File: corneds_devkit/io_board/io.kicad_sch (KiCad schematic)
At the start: 0 parts

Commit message: added switch footprint, io sch, and keypad IC footprint. Need to find new LEDs and make joystick footprint
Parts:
- added J1: Conn_02x10_Counter_Clockwise, Connector_PinHeader_1.27mm:PinHeader_2x10_P1.27mm_Horizontal, symbol Connector_Generic:Conn_02x10_Counter_Clockwise
- added J2, J3: Conn_01x03_Pin, Connector_PinHeader_1.27mm:PinHeader_1x03_P1.27mm_Vertical, symbol Connector:Conn_01x03_Pin
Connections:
- new net GNDL: J1.10 (Pin_10)
- new net GNDR: J1.11 (Pin_11)
- new net SCLL: J1.6 (Pin_6)
- new net SCLR: J1.15 (Pin_15)
- new net SDAL: J1.5 (Pin_5)
- new net SDAR: J1.16 (Pin_16)
- new net VDD_3V3L: J1.2 (Pin_2), J2.1 (Pin_1)
- new net VDD_3V3R: J1.19 (Pin_19), J3.3 (Pin_3)
- new net VDD_5VL: J1.1 (Pin_1), J2.3 (Pin_3)
- new net VDD_5VR: J1.20 (Pin_20), J3.1 (Pin_1)
- new net VJOYL: J2.2 (Pin_2)
- new net VJOYR: J3.2 (Pin_2)
- new net left_led_di: J1.3 (Pin_3)
- new net mouse_x: J1.13 (Pin_13)
- new net mouse_y: J1.14 (Pin_14)
- new net nINTL: J1.4 (Pin_4)
- new net nINTR: J1.17 (Pin_17)
- new net nRESET: J1.9 (Pin_9)
- new net right_led_di: J1.18 (Pin_18)
- new net scroll_x: J1.8 (Pin_8)
- new net scroll_y: J1.7 (Pin_7)

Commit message: io sch done. Need to route
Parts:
- added J4: nOEL_en, Connector_PinHeader_1.00mm:PinHeader_1x02_P1.00mm_Vertical, symbol Connector:Conn_01x02_Pin
- added J5: nOER_en, Connector_PinHeader_1.00mm:PinHeader_1x02_P1.00mm_Vertical, symbol Connector:Conn_01x02_Pin
- added R10, R4, R6, R8: 20k, Resistor_SMD:R_0402_1005Metric, symbol Device:R
- added R3, R5, R7, R9: 10k, Resistor_SMD:R_0402_1005Metric, symbol Device:R
- added U5, U6: TXB0102DCU, Package_SO:VSSOP-8_2.4x2.1mm_P0.5mm, symbol Logic_LevelTranslator:TXB0102DCU
- J2: value Conn_01x03_Pin -> JOYL_VSEL
- J3: value Conn_01x03_Pin -> JOYR_VSEL
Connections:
- net GNDL: now also J4.2 (Pin_2), R4.2, R6.2, U5.2 (GND)
- net GNDR: now also J5.1 (Pin_1), R10.2, R8.2, U6.2 (GND)
- net VDD_3V3L: now also U5.3 (VCCA)
- net VDD_3V3R: now also U6.3 (VCCA)
- net VDD_5VL: now also U5.7 (VCCB)
- net VDD_5VR: now also U6.7 (VCCB)
- net left_led_di: now also U5.8 (B1); no longer J1.3 (Pin_3)
- net mouse_x: now also R9.1; no longer J1.13 (Pin_13)
- net mouse_y: now also R7.1; no longer J1.14 (Pin_14)
- net right_led_di: now also U6.8 (B1); no longer J1.18 (Pin_18)
- net scroll_x: now also R5.1; no longer J1.8 (Pin_8)
- net scroll_y: now also R3.1; no longer J1.7 (Pin_7)
- new net: J1.8 (Pin_8), R3.2, R4.1
- new net: J1.3 (Pin_3), U5.5 (A1)
- new net: J4.1 (Pin_1), U5.6 (OE)
- new net: J1.7 (Pin_7), R5.2, R6.1
- new net: J1.13 (Pin_13), R10.1, R9.2
- new net: J1.14 (Pin_14), R7.2, R8.1
- new net: J1.18 (Pin_18), U6.5 (A1)
- new net: J5.2 (Pin_2), U6.6 (OE)
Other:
- moved on the sheet: J1, J2, J3

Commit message: finished routing power board and started on control board schematic but realized I need seperate reset lines
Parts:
- J1: footprint Connector_PinHeader_1.27mm:PinHeader_2x10_P1.27mm_Horizontal -> Connector_PinHeader_1.27mm:PinHeader_2x10_P1.27mm_Vertical
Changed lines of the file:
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@@
 			)
 		)
-		(property "Footprint" "Connector_PinHeader_1.27mm:PinHeader_2x10_P1.27mm_Horizontal"
+		(property "Footprint" "Connector_PinHeader_1.27mm:PinHeader_2x10_P1.27mm_Vertical"
 			(at 157.48 63.5 0)
 			(effects

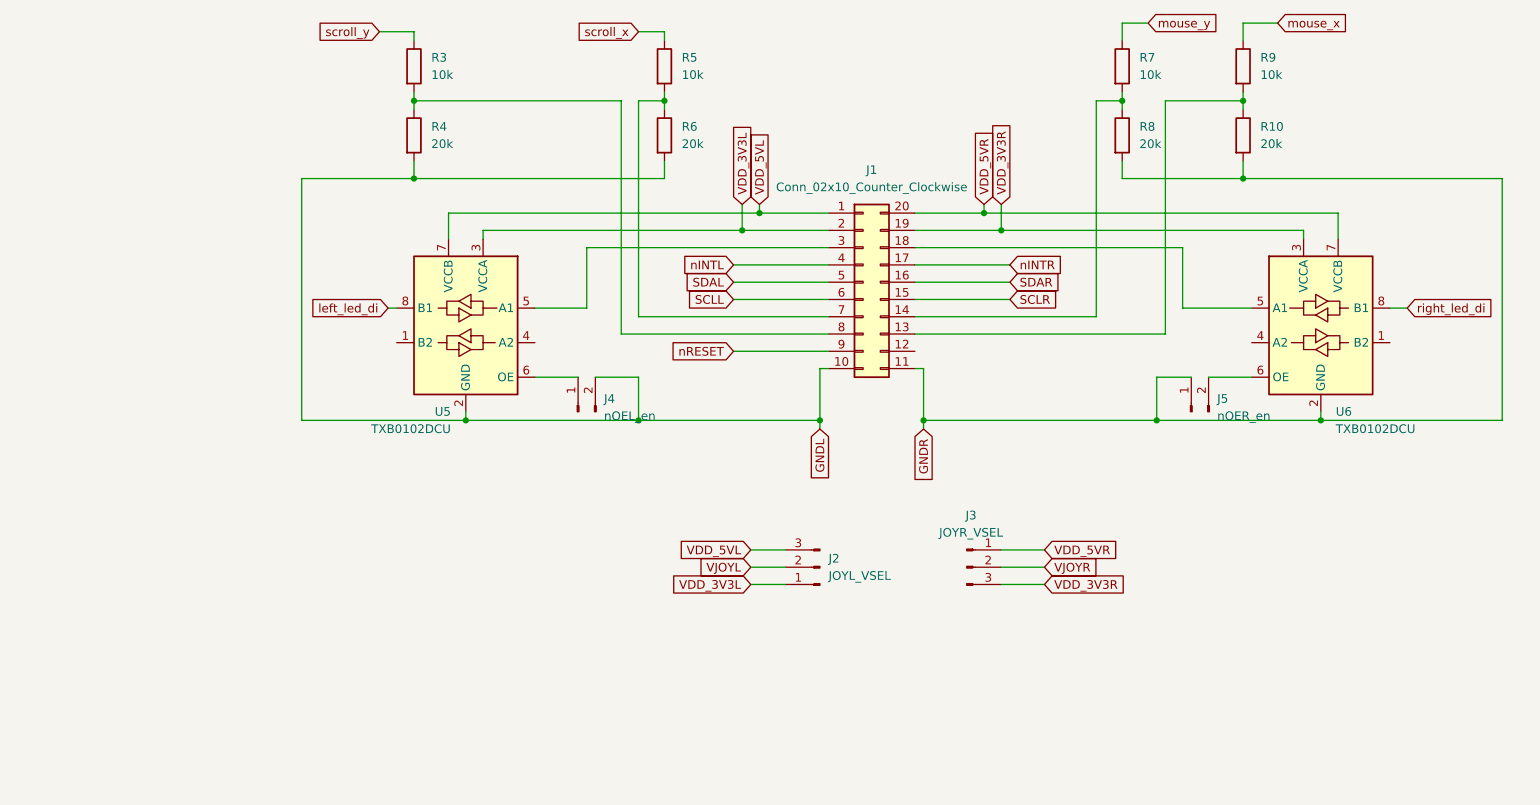
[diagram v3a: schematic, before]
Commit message: ordered devkit rev A
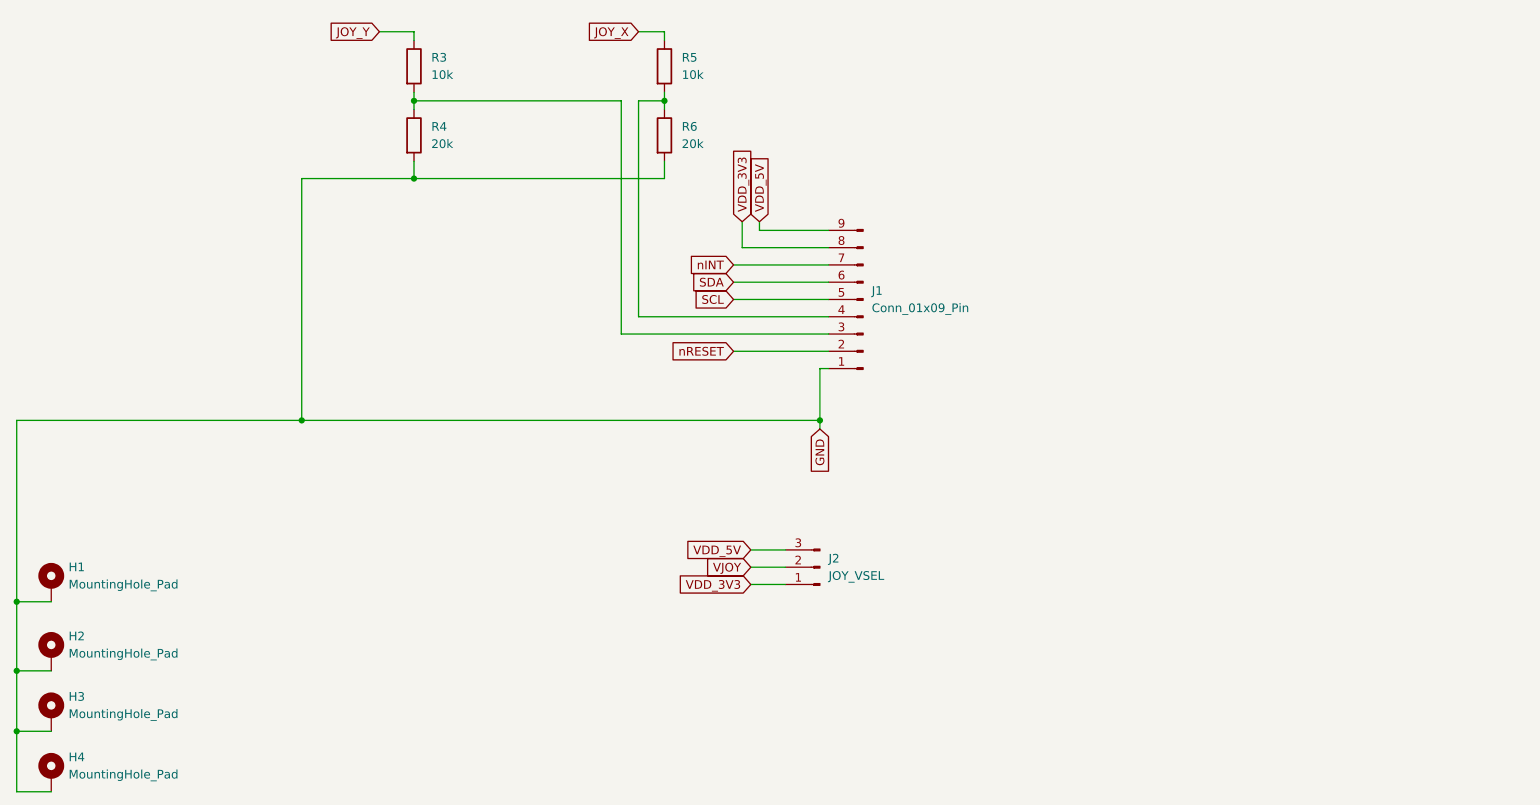
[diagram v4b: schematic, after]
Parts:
- removed J1: Conn_02x10_Counter_Clockwise, Connector_PinHeader_1.27mm:PinHeader_2x10_P1.27mm_Vertical, symbol Connector_Generic:Conn_02x10_Counter_Clockwise
- removed J3: JOYR_VSEL, Connector_PinHeader_1.27mm:PinHeader_1x03_P1.27mm_Vertical, symbol Connector:Conn_01x03_Pin
- removed J4: nOEL_en, Connector_PinHeader_1.00mm:PinHeader_1x02_P1.00mm_Vertical, symbol Connector:Conn_01x02_Pin
- removed J5: nOER_en, Connector_PinHeader_1.00mm:PinHeader_1x02_P1.00mm_Vertical, symbol Connector:Conn_01x02_Pin
- removed R10, R8: 20k, Resistor_SMD:R_0402_1005Metric, symbol Device:R
- removed R7, R9: 10k, Resistor_SMD:R_0402_1005Metric, symbol Device:R
- removed U5, U6: TXB0102DCU, Package_SO:VSSOP-8_2.4x2.1mm_P0.5mm, symbol Logic_LevelTranslator:TXB0102DCU
- added H1, H2, H3, H4: MountingHole_Pad, MountingHole:MountingHole_3.2mm_M3_Pad_Via, symbol Mechanical:MountingHole_Pad
- added J1: Conn_01x09_Pin, Connector_PinHeader_1.27mm:PinHeader_1x09_P1.27mm_Vertical, symbol Connector:Conn_01x09_Pin
- J2: value JOYL_VSEL -> JOY_VSEL
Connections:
- net nRESET: now also J1.2 (Pin_2)
- net at R3.2, R4.1: now also J1.3 (Pin_3)
- net at R5.2, R6.1: now also J1.4 (Pin_4)
- net GNDL renamed GND
- net GND: now also H1.1, H2.1, H3.1, H4.1, J1.1 (Pin_1)
- net VDD_3V3L renamed VDD_3V3
- net VDD_3V3: now also J1.8 (Pin_8)
- net VDD_5VL renamed VDD_5V
- net VDD_5V: now also J1.9 (Pin_9)
- net VJOYL renamed VJOY
- net scroll_x renamed JOY_X
- net scroll_y renamed JOY_Y
- new net SCL: J1.5 (Pin_5)
- new net SDA: J1.6 (Pin_6)
- new net nINT: J1.7 (Pin_7)
